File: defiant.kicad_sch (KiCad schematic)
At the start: 42 parts, among them J1 Conn_01x02_Pin, U1 Seeed Studio XIAO BLE

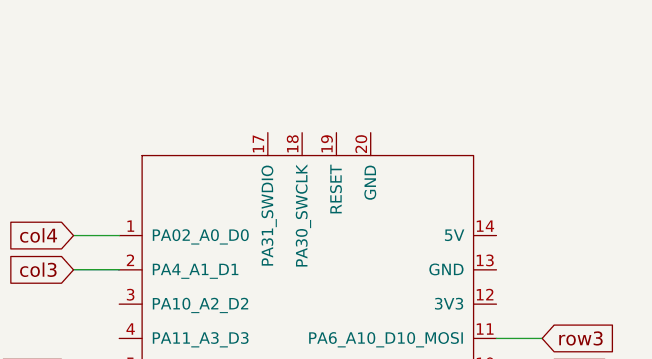
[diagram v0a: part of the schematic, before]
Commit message: Change thumb pad to regular keys
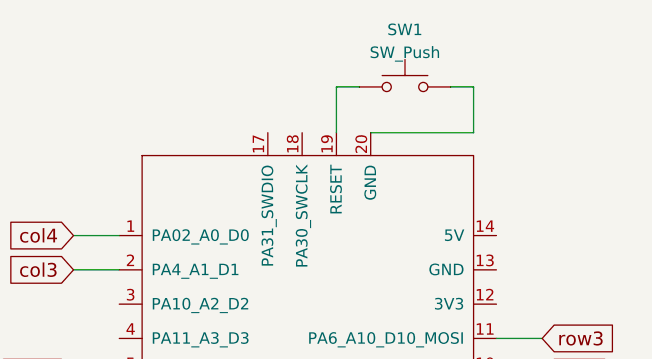
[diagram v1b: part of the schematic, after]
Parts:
- added SW1: SW_Push, symbol Switch:SW_Push
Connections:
- net at U1.19 (RESET): now also SW1.1
- net at U1.20 (GND): now also SW1.2
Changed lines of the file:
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@@
+    (stroke (width 0) (type default))
+  )
+  (wire (pts (xy 232.41 33.02) (xy 243.84 33.02))
     (stroke (width 0) (type default))
   )
@@
     (stroke (width 0) (type default))
   )
+  (wire (pts (xy 228.6 33.02) (xy 228.6 27.94))
+    (stroke (width 0) (type default))
+  )
+  (wire (pts (xy 243.84 27.94) (xy 241.3 27.94))
+    (stroke (width 0) (type default))
+  )
   (wire (pts (xy 120.65 85.09) (xy 143.51 85.09))
     (stroke (width 0) (type default))
@@
     (stroke (width 0) (type default))
   )
+  (wire (pts (xy 243.84 33.02) (xy 243.84 27.94))
+    (stroke (width 0) (type default))
+  )
   (wire (pts (xy 59.69 95.25) (xy 36.83 95.25))
+    (stroke (width 0) (type default))
+  )
+  (wire (pts (xy 228.6 27.94) (xy 231.14 27.94))
     (stroke (width 0) (type default))
   )
@@
         )
       )
+    )
+  )
+  (symbol (lib_id "Switch:SW_Push") (at 236.22 27.94 0) (unit 1)
+    (in_bom yes) (on_board yes) (dnp no) (fields_autoplaced)
+    (property "Reference" "SW1" (at 236.22 21.59 0)
+      (effects (font (size 1.27 1.27)))
+    )
+    (property "Value" "SW_Push" (at 236.22 24.13 0)
+      (effects (font (size 1.27 1.27)))
+    )
+    (property "Footprint" "" (at 236.22 22.86 0)
+      (effects (font (size 1.27 1.27)) hide)
+    )
+    (property "Datasheet" "~" (at 236.22 22.86 0)
+      (effects (font (size 1.27 1.27)) hide)
+    )
+    (pin "1")
+    (pin "2")
+    (instances
+      (project "defiant"
+        (path "/cd54289a-7f2f-4953-8338-a5e4a81fda5f"
+          (reference "SW1") (unit 1)
+        )
+      )

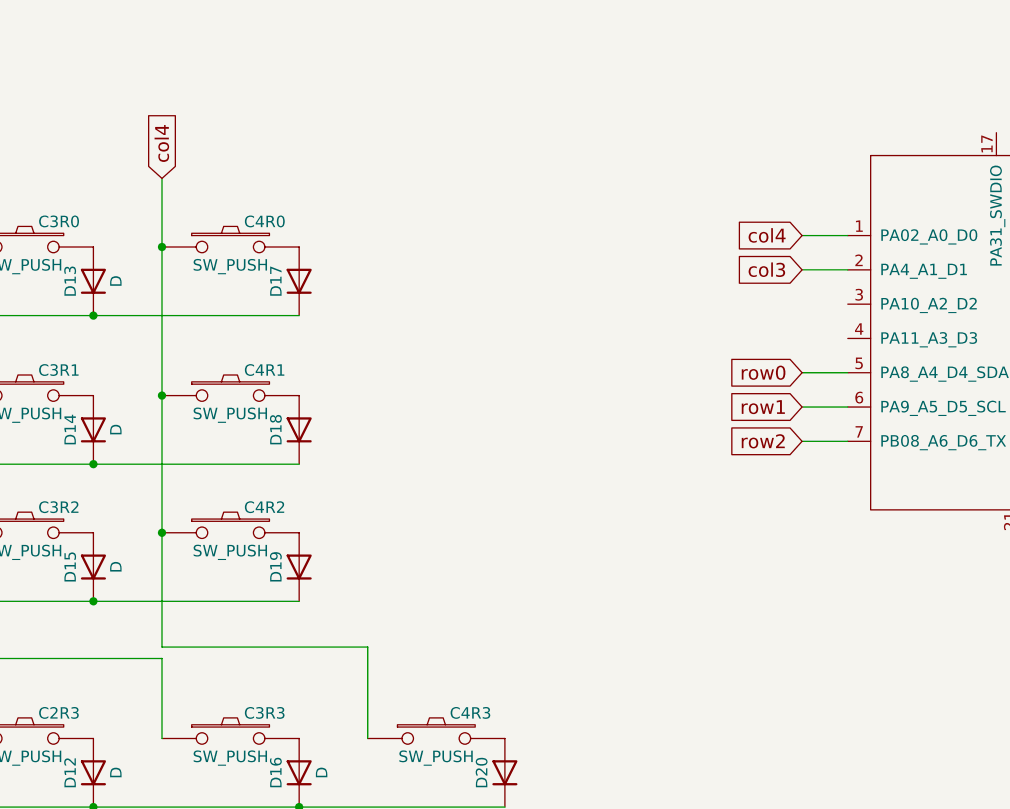
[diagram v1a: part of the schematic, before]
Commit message: Update footprints
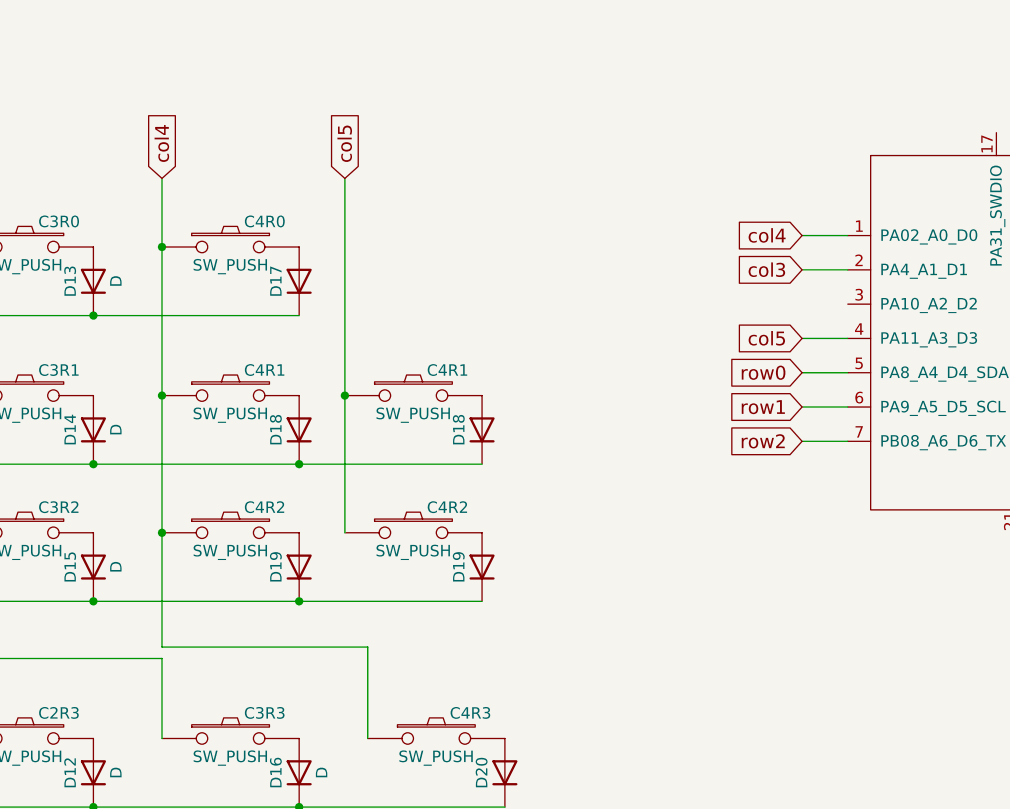
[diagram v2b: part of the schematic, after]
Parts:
- added C4R1, C4R2: SW_PUSH, Defiant:SW_Gateron_LowProfile_HotSwap_PTH_Reversible, symbol corne-chocolate-rescue:SW_PUSH-kbd
- added D18, D19: D, Diode_SMD:D_SOD-123, symbol Device:D
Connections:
- net row1: now also D18.1 (K)
- net row2: now also D19.1 (K)
- net col5: now reaches U1.4 (PA11_A3_D3)
- net col5: now also C4R1.1, C4R2.1
- new net: C4R1.2, D18.2 (A)
- new net: C4R2.2, D19.2 (A)
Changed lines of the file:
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@@
   (junction (at 74.93 69.85) (diameter 0) (color 0 0 0 0)
   )
+  (junction (at 143.51 69.85) (diameter 0) (color 0 0 0 0)
+  )
   (junction (at 59.69 45.72) (diameter 0) (color 0 0 0 0)
   )
@@
   (junction (at 82.55 45.72) (diameter 0) (color 0 0 0 0)
   )
+  (junction (at 143.51 85.09) (diameter 0) (color 0 0 0 0)
+  )
   (junction (at 74.93 85.09) (diameter 0) (color 0 0 0 0)
   )
@@
   (junction (at 97.79 85.09) (diameter 0) (color 0 0 0 0)
   )
+  (junction (at 148.59 62.23) (diameter 0) (color 0 0 0 0)
+  )
   (junction (at 120.65 85.09) (diameter 0) (color 0 0 0 0)
   )
@@
     (stroke (width 0) (type default))
   )
+  (wire (pts (xy 128.27 90.17) (xy 151.13 90.17))
+    (stroke (width 0) (type default))
+  )
   (wire (pts (xy 251.46 55.88) (xy 246.38 55.88))
     (stroke (width 0) (type default))
@@
     (stroke (width 0) (type default))
   )
+  (wire (pts (xy 148.59 62.23) (xy 148.59 77.47))
+    (stroke (width 0) (type default))
+  )
   (wire (pts (xy 97.79 69.85) (xy 120.65 69.85))
     (stroke (width 0) (type default))
@@
     (stroke (width 0) (type default))
   )
+  (wire (pts (xy 143.51 69.85) (xy 163.83 69.85))
+    (stroke (width 0) (type default))
+  )
   (wire (pts (xy 82.55 93.98) (xy 82.55 100.33))
     (stroke (width 0) (type default))
@@
     (stroke (width 0) (type default))
   )
-  (wire (pts (xy 151.13 90.17) (xy 128.27 90.17))
-    (stroke (width 0) (type default))
-  )
   (wire (pts (xy 82.55 45.72) (xy 82.55 62.23))
     (stroke (width 0) (type default))
@@
     (stroke (width 0) (type default))
   )
+  (wire (pts (xy 143.51 85.09) (xy 163.83 85.09))
+    (stroke (width 0) (type default))
+  )
+  (wire (pts (xy 199.39 55.88) (xy 204.47 55.88))
+    (stroke (width 0) (type default))
+  )
   (wire (pts (xy 128.27 91.44) (xy 105.41 91.44))
     (stroke (width 0) (type default))
@@
   )
   (wire (pts (xy 36.83 38.1) (xy 36.83 45.72))
+    (stroke (width 0) (type default))
+  )
+  (wire (pts (xy 148.59 38.1) (xy 148.59 62.23))
     (stroke (width 0) (type default))
   )
@@
     (effects (font (size 1.524 1.524)) (justify right))
     (property "Intersheetrefs" "${INTERSHEET_REFS}" (at 199.39 48.26 0)
+      (effects (font (size 1.27 1.27)) hide)
+    )
+  )
+  (global_label "col5" (shape input) (at 199.39 55.88 180)
+    (effects (font (size 1.524 1.524)) (justify right))
+    (property "Intersheetrefs" "${INTERSHEET_REFS}" (at 199.39 55.88 0)
       (effects (font (size 1.27 1.27)) hide)
     )
@@
     )
   )
+  (global_label "col5" (shape input) (at 148.59 38.1 90)
+    (effects (font (size 1.524 1.524)) (justify left))
+    (property "Intersheetrefs" "${INTERSHEET_REFS}" (at 148.59 38.1 0)
+      (effects (font (size 1.27 1.27)) hide)
+    )
+  )
   (global_label "col2" (shape input) (at 251.46 67.31 0)
     (effects (font (size 1.524 1.524)) (justify left))
@@
     )
   )
+  (symbol (lib_id "Device:D") (at 163.83 66.04 90) (unit 1)
+    (in_bom yes) (on_board yes) (dnp no)
+    (property "Reference" "D18" (at 161.29 66.04 0)
+      (effects (font (size 1.27 1.27)))
+    )
+    (property "Value" "D" (at 166.37 66.04 0)
+      (effects (font (size 1.27 1.27)) hide)
+    )
+    (property "Footprint" "Diode_SMD:D_SOD-123" (at 163.83 66.04 0)
+      (effects (font (size 1.27 1.27)) hide)
+    )
+    (property "Datasheet" "" (at 163.83 66.04 0)
+      (effects (font (size 1.27 1.27)) hide)
+    )
+    (pin "1")
+    (pin "2")
+    (instances
+      (project "flat-wedge"
+        (path "/7f5ded0f-6aaa-4ef3-b847-f44e901064a1"
+          (reference "D18") (unit 1)
+        )
+      )
+      (project "the-wedge"
+        (path "/a781ce2d-1f88-403d-98c4-fb403b1f974e"
+          (reference "D10") (unit 1)
+        )
+      )
+      (project "defiant"
+        (path "/cd54289a-7f2f-4953-8338-a5e4a81fda5f"
+          (reference "D22") (unit 1)
+        )
+      )
+    )
+  )
   (symbol (lib_id "Device:D") (at 166.37 104.14 90) (unit 1)
     (in_bom yes) (on_board yes) (dnp no)
@@
         (path "/cd54289a-7f2f-4953-8338-a5e4a81fda5f"
           (reference "D20") (unit 1)
+        )
+      )
+    )
+  )
+  (symbol (lib_id "corne-chocolate-rescue:SW_PUSH-kbd") (at 156.21 62.23 0) (unit 1)
+    (in_bom yes) (on_board yes) (dnp no)
+    (property "Reference" "C4R1" (at 160.02 59.436 0)
+      (effects (font (size 1.27 1.27)))
+    )
+    (property "Value" "SW_PUSH" (at 156.21 64.262 0)
+      (effects (font (size 1.27 1.27)))
+    )
+    (property "Footprint" "Defiant:SW_Gateron_LowProfile_HotSwap_PTH_Reversible" (at 156.21 62.23 0)
+      (effects (font (size 1.27 1.27)) hide)
+    )
+    (property "Datasheet" "" (at 156.21 62.23 0)
+      (effects (font (size 1.27 1.27)))
+    )
+    (pin "1")
+    (pin "2")
+    (instances
+      (project "flat-wedge"
+        (path "/7f5ded0f-6aaa-4ef3-b847-f44e901064a1"
+          (reference "C4R1") (unit 1)
+        )
+      )
+      (project "the-wedge"
+        (path "/a781ce2d-1f88-403d-98c4-fb403b1f974e"
+          (reference "C4R1") (unit 1)
+        )
+      )
+      (project "defiant"
+        (path "/cd54289a-7f2f-4953-8338-a5e4a81fda5f"
+          (reference "C5R2") (unit 1)
         )
       )
@@
         (path "/cd54289a-7f2f-4953-8338-a5e4a81fda5f"
           (reference "C1R1") (unit 1)
+        )
+      )
+    )
+  )
+  (symbol (lib_id "corne-chocolate-rescue:SW_PUSH-kbd") (at 156.21 77.47 0) (unit 1)
+    (in_bom yes) (on_board yes) (dnp no)
+    (property "Reference" "C4R2" (at 160.02 74.676 0)
+      (effects (font (size 1.27 1.27)))
+    )
+    (property "Value" "SW_PUSH" (at 156.21 79.502 0)
+      (effects (font (size 1.27 1.27)))
+    )
+    (property "Footprint" "Defiant:SW_Gateron_LowProfile_HotSwap_PTH_Reversible" (at 156.21 77.47 0)
+      (effects (font (size 1.27 1.27)) hide)
+    )
+    (property "Datasheet" "" (at 156.21 77.47 0)
+      (effects (font (size 1.27 1.27)))
+    )
+    (pin "1")
+    (pin "2")
+    (instances
+      (project "flat-wedge"
+        (path "/7f5ded0f-6aaa-4ef3-b847-f44e901064a1"
+          (reference "C4R2") (unit 1)
+        )
+      )
+      (project "the-wedge"
+        (path "/a781ce2d-1f88-403d-98c4-fb403b1f974e"
+          (reference "C4R2") (unit 1)
+        )
+      )
+      (project "defiant"
+        (path "/cd54289a-7f2f-4953-8338-a5e4a81fda5f"
+          (reference "C5R3") (unit 1)
         )
       )
@@
         )
       )
+    )
+  )
+  (symbol (lib_id "Device:D") (at 163.83 81.28 90) (unit 1)
+    (in_bom yes) (on_board yes) (dnp no)
+    (property "Reference" "D19" (at 161.29 81.28 0)
+      (effects (font (size 1.27 1.27)))
+    )
+    (property "Value" "D" (at 166.37 81.28 0)
+      (effects (font (size 1.27 1.27)) hide)
+    )
+    (property "Footprint" "Diode_SMD:D_SOD-123" (at 163.83 81.28 0)
+      (effects (font (size 1.27 1.27)) hide)
+    )
+    (property "Datasheet" "" (at 163.83 81.28 0)
+      (effects (font (size 1.27 1.27)) hide)
+    )
+    (pin "1")
+    (pin "2")
+    (instances
+      (project "flat-wedge"
+        (path "/7f5ded0f-6aaa-4ef3-b847-f44e901064a1"
+          (reference "D19") (unit 1)
+        )
+      )
+      (project "the-wedge"
+        (path "/a781ce2d-1f88-403d-98c4-fb403b1f974e"
+          (reference "D14") (unit 1)
+        )
+      )
+      (project "defiant"
+        (path "/cd54289a-7f2f-4953-8338-a5e4a81fda5f"
+          (reference "D23") (unit 1)
+        )
+      )
